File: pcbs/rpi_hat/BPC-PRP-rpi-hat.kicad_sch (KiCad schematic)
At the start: 38 parts, among them J1 Power, J2 Power, J3 Fan_power, J4 I2C, J5 UART, J6 SPI, SW1 SW_DIP_x01, SW2 SW_DIP_x01, SW3 SW_DIP_x01, U3 DS3231M

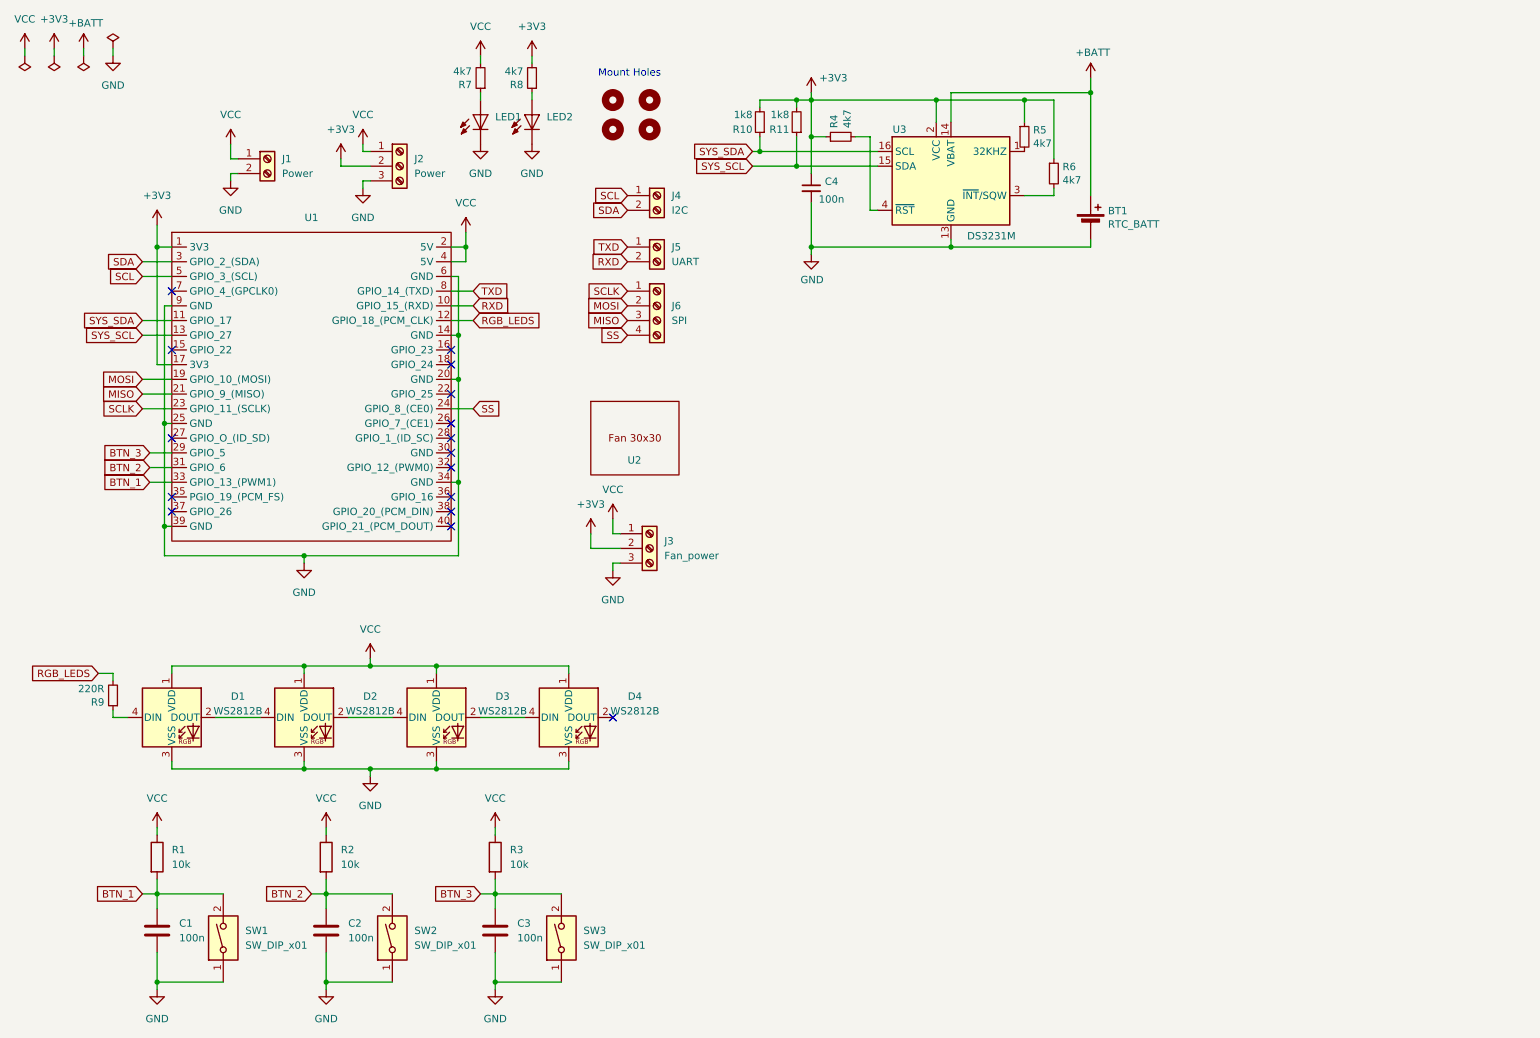
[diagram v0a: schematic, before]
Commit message: updated rpi ext board
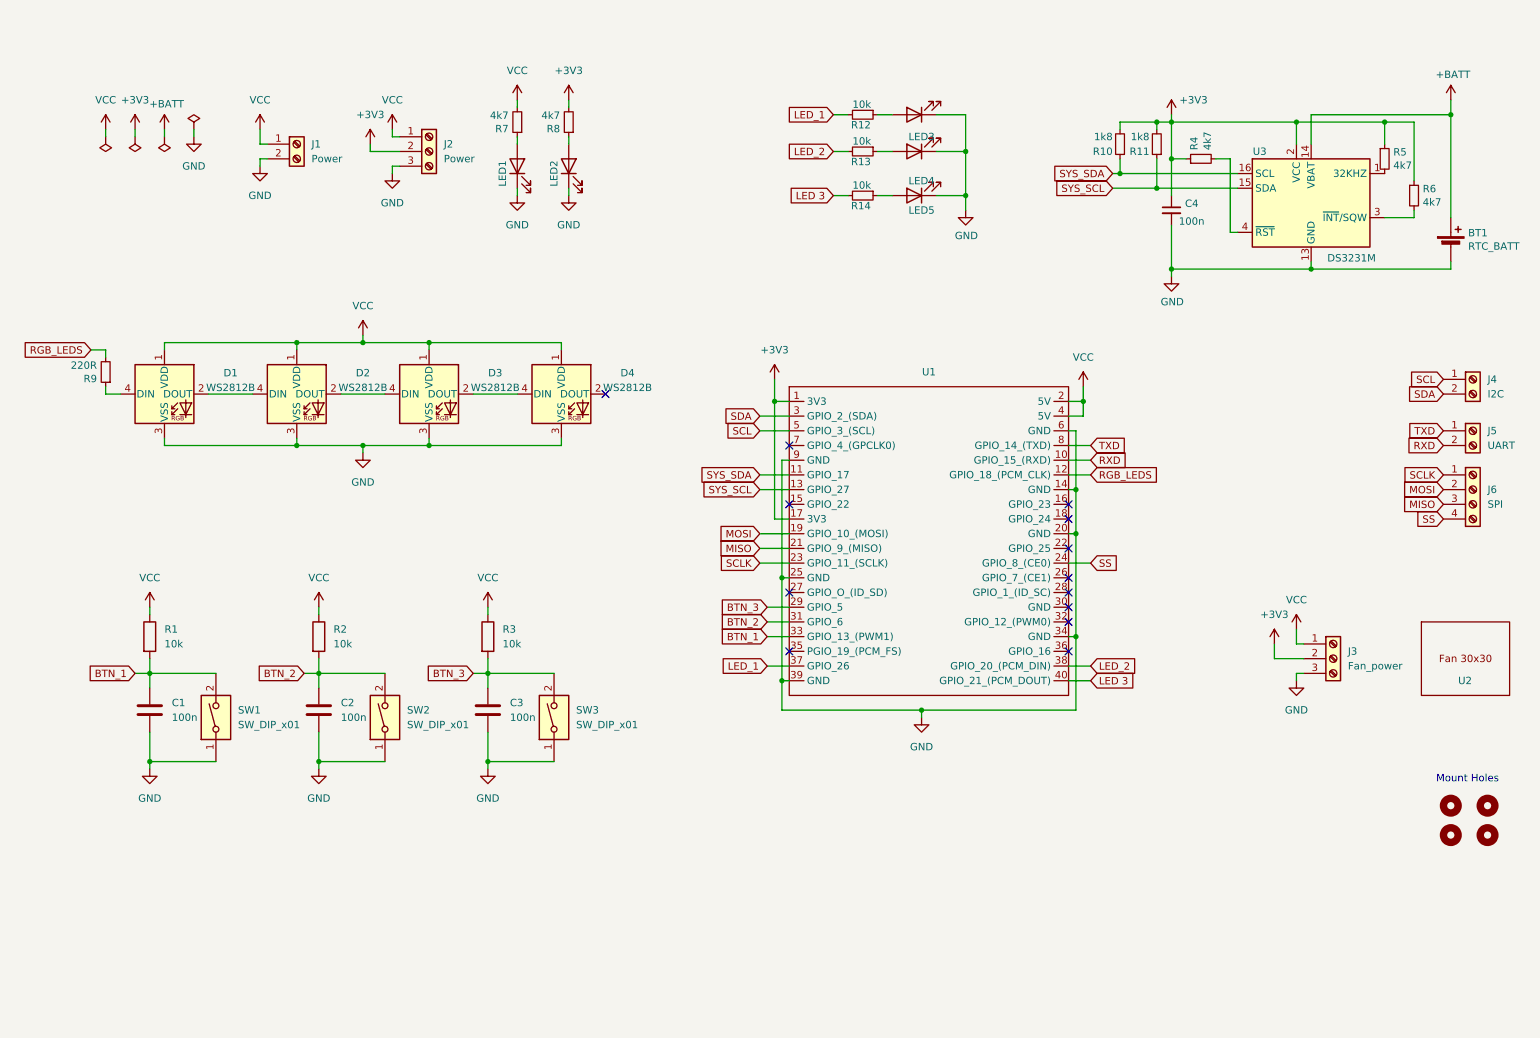
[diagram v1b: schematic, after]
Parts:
- removed LED1, LED2: ~, CHIPLED_1206, symbol adafruit:LEDCHIPLED_1206
- added LED1, LED2, LED3, LED4, LED5: ~, LED_SMD:LED_1206_3216Metric, symbol LED:IR26-21C_L110_TR8
- added R12, R13, R14: 10k, Resistor_SMD:R_1206_3216Metric, symbol Device:R_Small
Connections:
- net GND: now also LED1.1 (K), LED2.1 (K), LED3.1 (K), LED4.1 (K), LED5.1 (K)
- net at R7.1: now also LED1.2 (A)
- net LED_1: now reaches U1.37 (GPIO_26)
- net LED_1: now also R12.2
- net LED_2: now reaches U1.38 (GPIO_20_(PCM_DIN))
- net LED_2: now also R13.2
- net LED 3: now reaches U1.40 (GPIO_21_(PCM_DOUT))
- net LED 3: now also R14.2
- net at R8.1: now also LED2.2 (A)
- new net: LED4.2 (A), R13.1
- new net: LED3.2 (A), R12.1
- new net: LED5.2 (A), R14.1
- no-connect marks 16 -> 13
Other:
- moved on the sheet: BT1, C1, C2, C3, C4, D1, D2, D3, D4, J1, J2, J3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

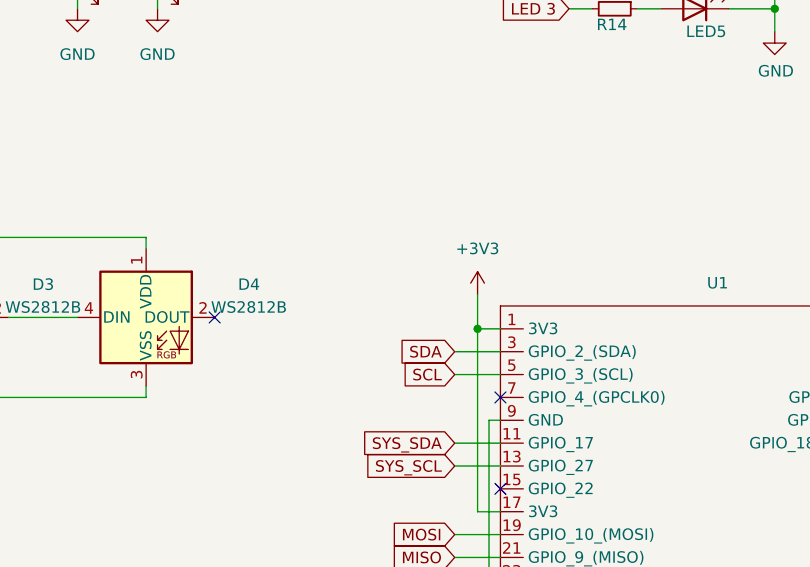
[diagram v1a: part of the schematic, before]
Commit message: add i2c pullups for rpi ext and i2c board
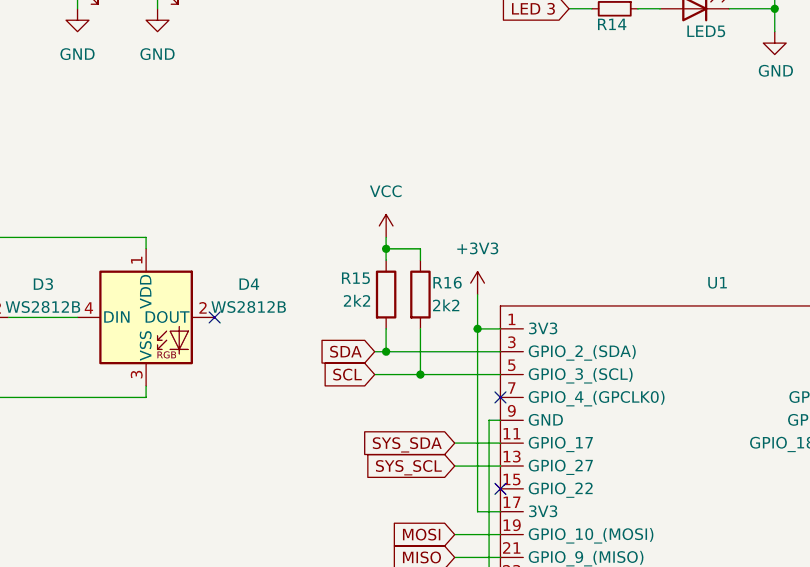
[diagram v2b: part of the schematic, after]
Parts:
- added R15, R16: 2k2, Resistor_SMD:R_1206_3216Metric, symbol Device:R
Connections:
- net SCL: now also R16.2
- net SDA: now also R15.2
- net VCC: now also R15.1, R16.1
